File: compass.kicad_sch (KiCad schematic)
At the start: 6 parts, among them U1201 LIS3MDL

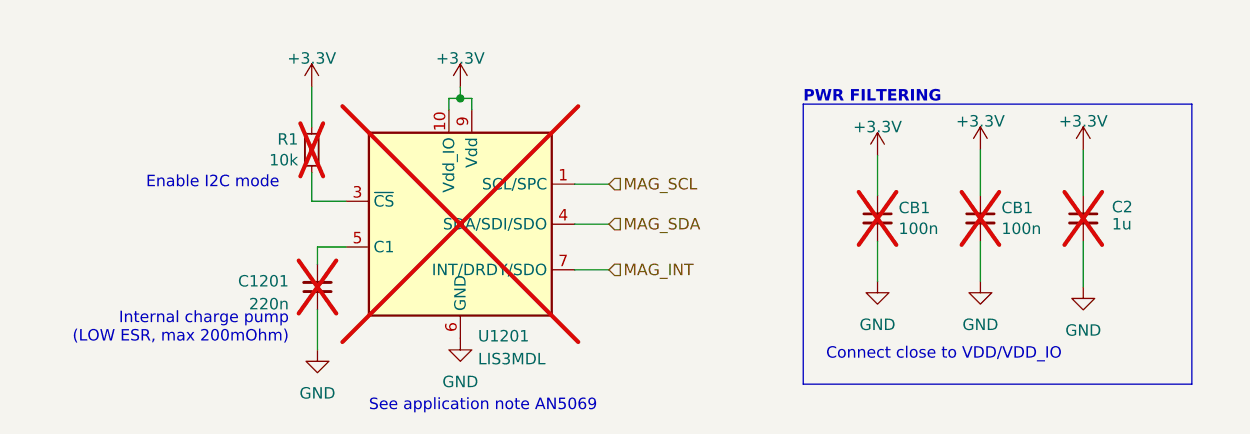
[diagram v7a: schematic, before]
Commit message: (sch) add I2C pull ups
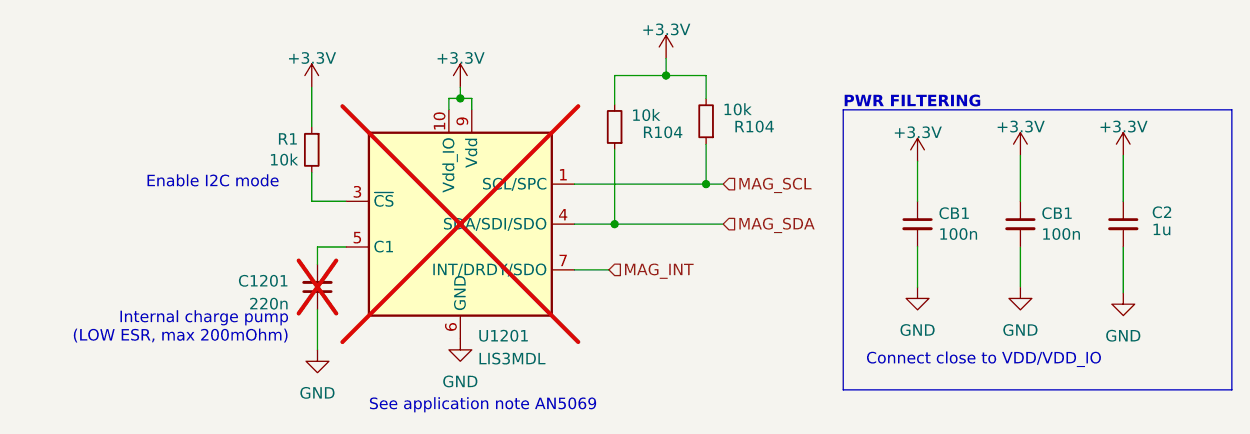
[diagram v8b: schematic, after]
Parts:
- added R104 (x2): 10k, Resistor_SMD:R_0402_1005Metric, symbol Device:R_Small
- C2, CB1, R1: now fitted
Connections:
- net +3.3V: now also R104.2, R104.2
- net MAG_SCL: now also R104.1
- net MAG_SDA: now also R104.1
